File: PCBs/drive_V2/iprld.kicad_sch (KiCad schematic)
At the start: 77 parts, among them IC1 W25Q16JVUXIQ_TR, IC2 ADS1115IDGSR, J1 SM06B-GHS-TB_LF__SN_, J10 XT60PW-F, J12 TYPE-C-31-M-12, J2 SM06B-GHS-TB_LF__SN_, J3 SM06B-GHS-TB_LF__SN_, J4 SM06B-GHS-TB_LF__SN_, J5 SM06B-GHS-TB_LF__SN_, J6 XT60PW-F, J7 SM06B-GHS-TB_LF__SN_, J8 XT60PW-F, J9 XT30PW-F, U1 AMS1117-3.3, U11 4N35, U12 4N35, U13 4N35, U14 4N35, U2 ESP32-S3, U3 4N35, U4 USBLC6-4SC6, U5 TCA9548APWR, U6 4N35, U7 4N35, U8 4N35, U9 AMS1117-5.0, Y1 7M40000010

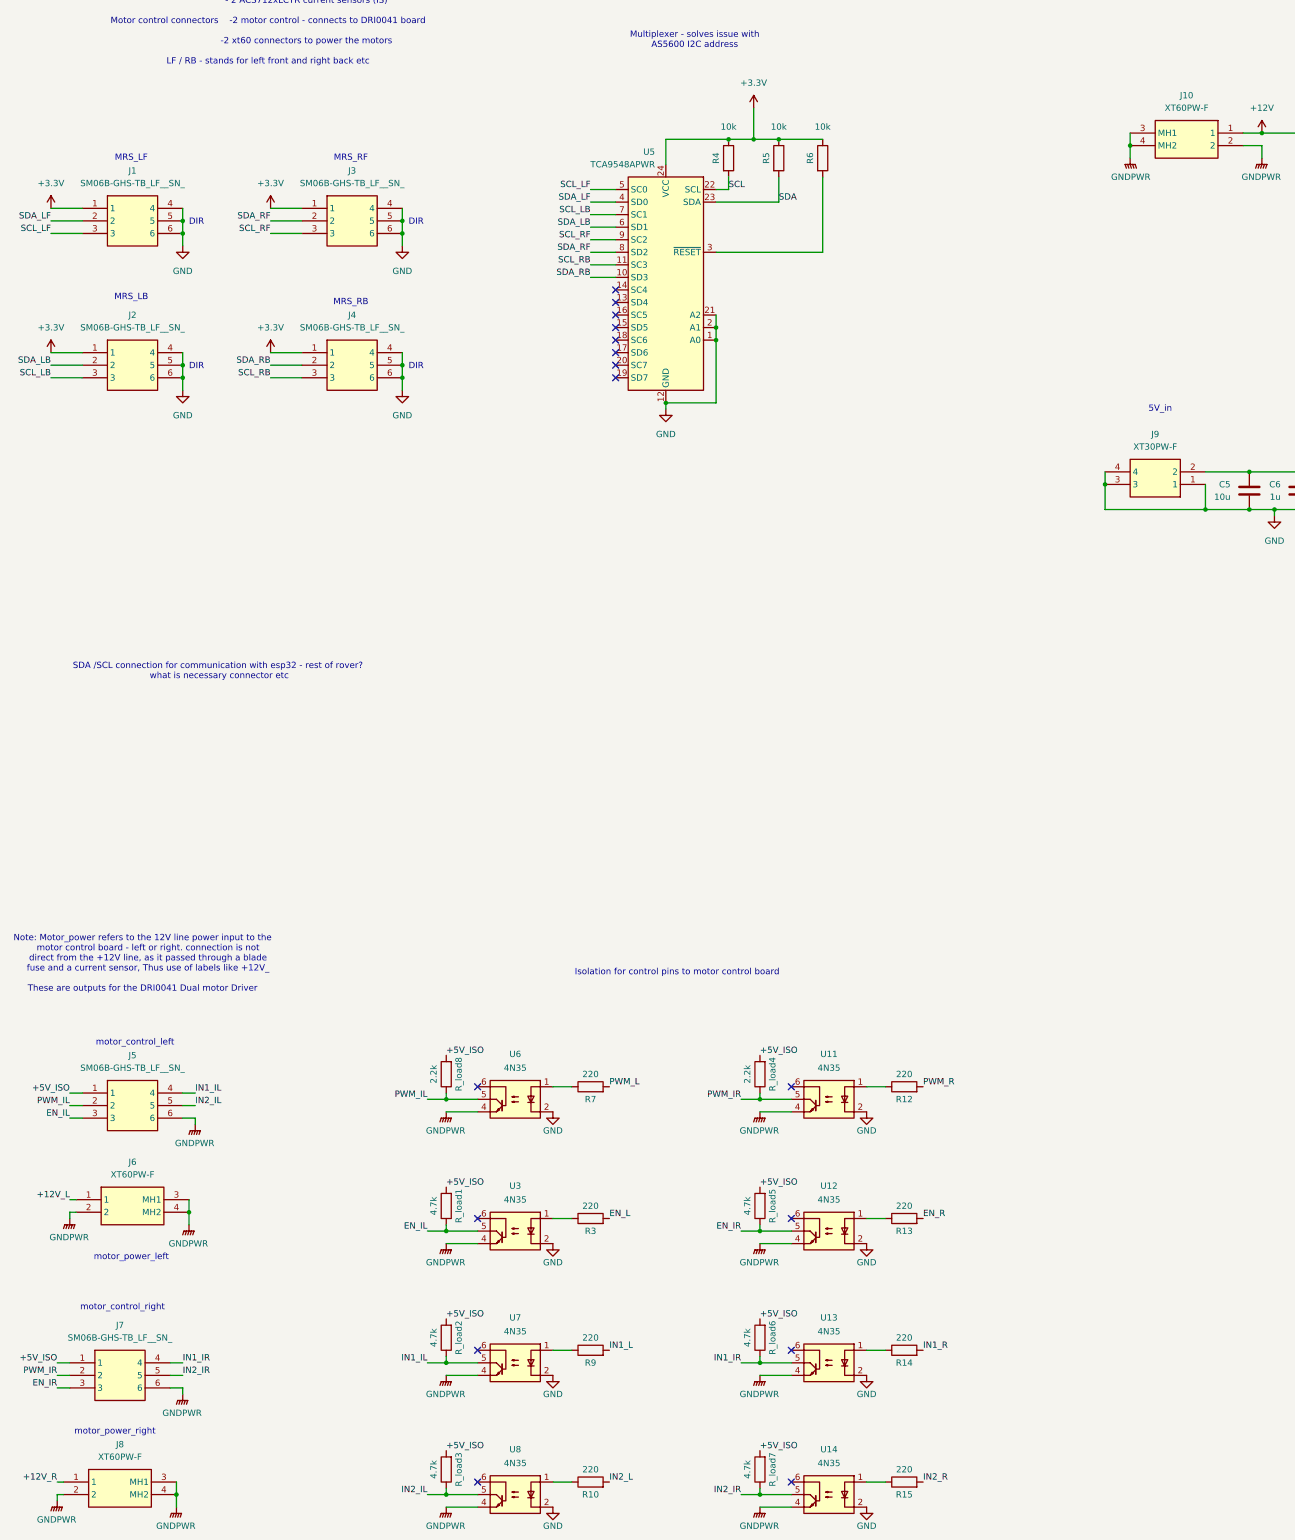
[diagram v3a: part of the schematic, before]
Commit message: added connector names
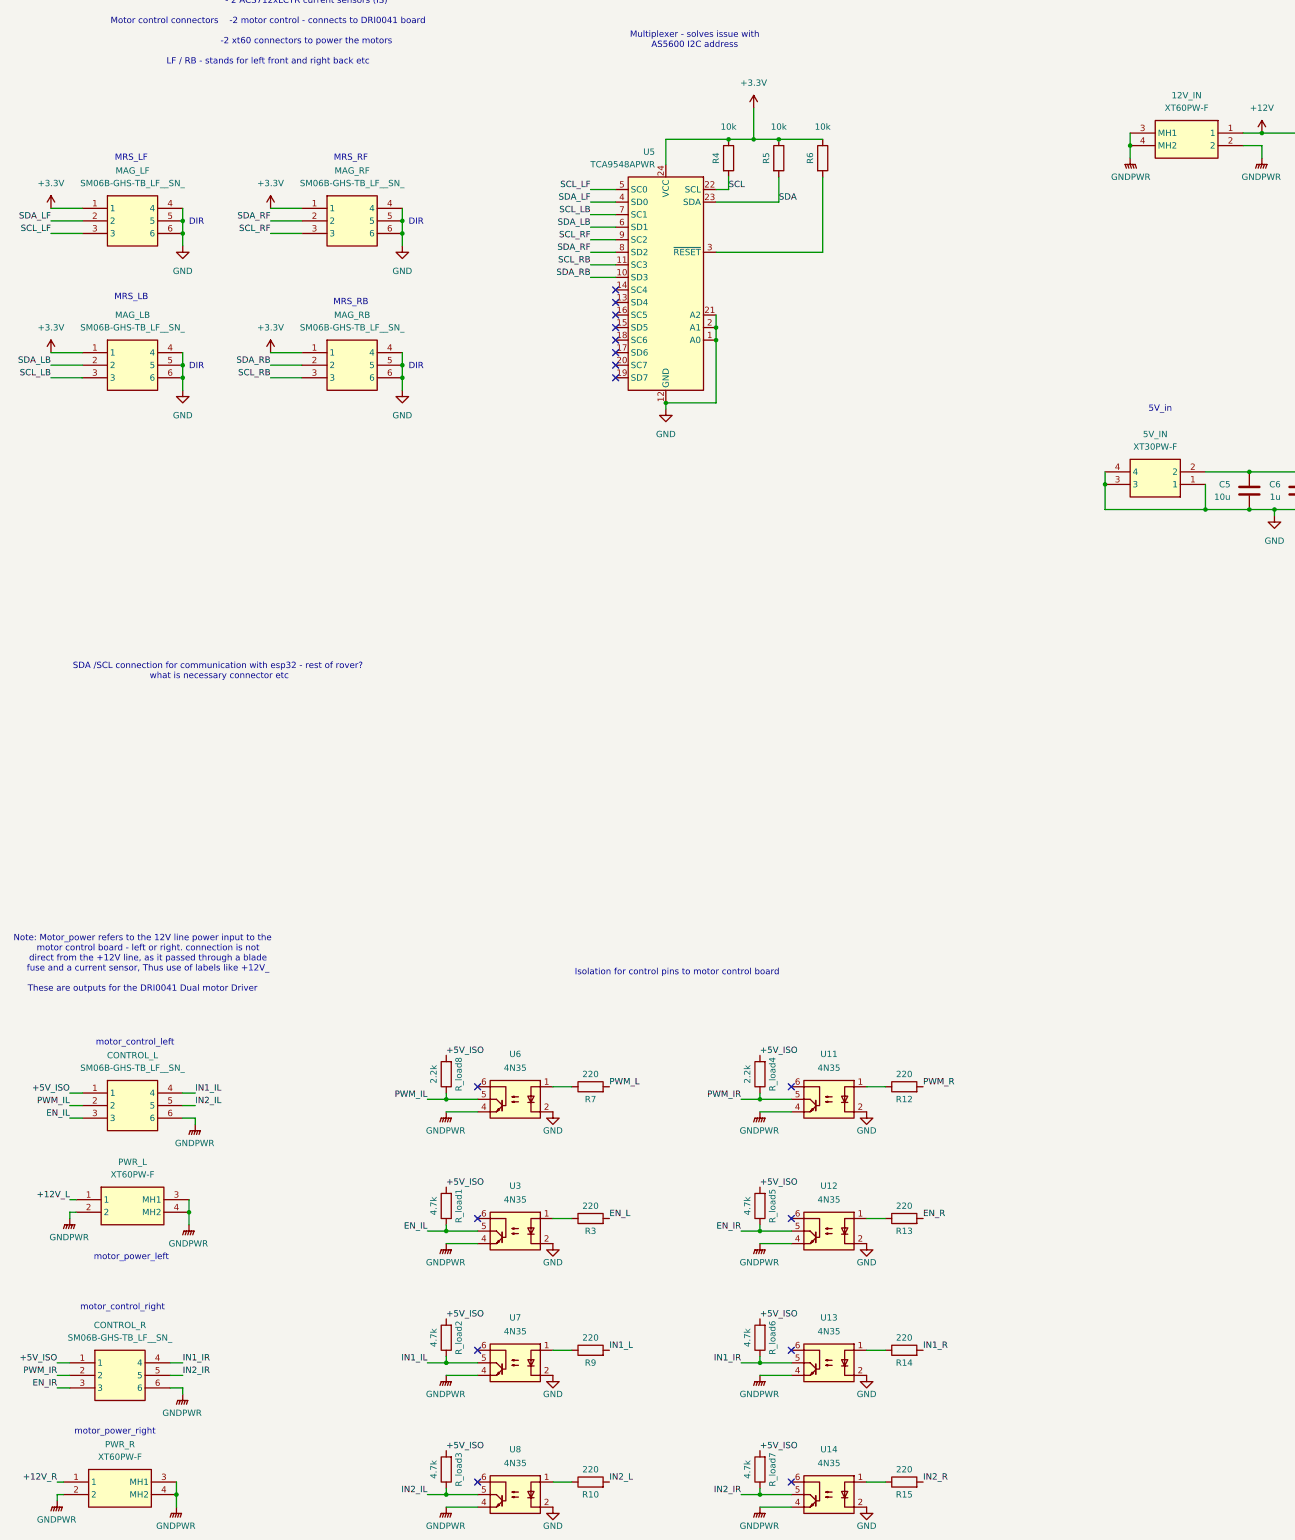
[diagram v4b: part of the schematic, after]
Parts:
- renumbered J10 to 12V_IN, J9 to 5V_IN, J5 to CONTROL_L, J7 to CONTROL_R, J2 to MAG_LB, J1 to MAG_LF, J4 to MAG_RB, J3 to MAG_RF, J6 to PWR_L, J8 to PWR_R
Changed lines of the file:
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@@
 		(on_board yes)
 		(dnp no)
-		(property "Reference" "J8"
+		(property "Reference" "PWR_R"
 			(at 57.15 342.9 0)
 			(effects
@@
 			(project "iprld"
 				(path "/f88582ba-beb9-4fb5-aa18-f7c4bf4c6866"
-					(reference "J8")
+					(reference "PWR_R")
 					(unit 1)
 				)
@@
 		(dnp no)
 		(fields_autoplaced yes)
-		(property "Reference" "J9"
+		(property "Reference" "5V_IN"
 			(at 266.7 138.43 0)
 			(effects
@@
 			(project "iprld"
 				(path "/f88582ba-beb9-4fb5-aa18-f7c4bf4c6866"
-					(reference "J9")
+					(reference "5V_IN")
 					(unit 1)
 				)
@@
 		(dnp no)
 		(fields_autoplaced yes)
-		(property "Reference" "J3"
+		(property "Reference" "MAG_RF"
 			(at 104.14 85.09 0)
 			(effects
@@
 			(project "iprld"
 				(path "/f88582ba-beb9-4fb5-aa18-f7c4bf4c6866"
-					(reference "J3")
+					(reference "MAG_RF")
 					(unit 1)
 				)
@@
 		(dnp no)
 		(fields_autoplaced yes)
-		(property "Reference" "J7"
+		(property "Reference" "CONTROL_R"
 			(at 57.15 318.77 0)
 			(effects
@@
 			(project "iprld"
 				(path "/f88582ba-beb9-4fb5-aa18-f7c4bf4c6866"
-					(reference "J7")
+					(reference "CONTROL_R")
 					(unit 1)
 				)
@@
 		(dnp no)
 		(fields_autoplaced yes)
-		(property "Reference" "J5"
+		(property "Reference" "CONTROL_L"
 			(at 59.69 264.16 0)
 			(effects
@@
 			(project "iprld"
 				(path "/f88582ba-beb9-4fb5-aa18-f7c4bf4c6866"
-					(reference "J5")
+					(reference "CONTROL_L")
 					(unit 1)
 				)
@@
 		(dnp no)
 		(fields_autoplaced yes)
-		(property "Reference" "J2"
+		(property "Reference" "MAG_LB"
 			(at 59.69 114.3 0)
 			(effects
@@
 			(project "iprld"
 				(path "/f88582ba-beb9-4fb5-aa18-f7c4bf4c6866"
-					(reference "J2")
+					(reference "MAG_LB")
 					(unit 1)
 				)
@@
 		(dnp no)
 		(fields_autoplaced yes)
-		(property "Reference" "J4"
+		(property "Reference" "MAG_RB"
 			(at 104.14 114.3 0)
 			(effects
@@
 			(project "iprld"
 				(path "/f88582ba-beb9-4fb5-aa18-f7c4bf4c6866"
-					(reference "J4")
+					(reference "MAG_RB")
 					(unit 1)
 				)
@@
 		(dnp no)
 		(fields_autoplaced yes)
-		(property "Reference" "J1"
+		(property "Reference" "MAG_LF"
 			(at 59.69 85.09 0)
 			(effects
@@
 			(project "iprld"
 				(path "/f88582ba-beb9-4fb5-aa18-f7c4bf4c6866"
-					(reference "J1")
+					(reference "MAG_LF")
 					(unit 1)
 				)
@@
 		(on_board yes)
 		(dnp no)
-		(property "Reference" "J10"
+		(property "Reference" "12V_IN"
 			(at 273.05 69.85 0)
 			(effects
@@
 			(project "iprld"
 				(path "/f88582ba-beb9-4fb5-aa18-f7c4bf4c6866"
-					(reference "J10")
+					(reference "12V_IN")
 					(unit 1)
 				)
@@
 		(on_board yes)
 		(dnp no)
-		(property "Reference" "J6"
+		(property "Reference" "PWR_L"
 			(at 59.69 285.75 0)
 			(effects
@@
 			(project "iprld"
 				(path "/f88582ba-beb9-4fb5-aa18-f7c4bf4c6866"
-					(reference "J6")
+					(reference "PWR_L")
 					(unit 1)
 				)

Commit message: Fixed some DRC errors
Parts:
- removed J12: TYPE-C-31-M-12, main_lib:TYPE-C-31-M-12, symbol TYPE-C-31-M-12:TYPE-C-31-M-12
- added J1: TYPE-C-31-M-12, iprl_footprints:TYPE-C-31-M-12, symbol TYPE-C-31-M-12:TYPE-C-31-M-12
- renumbered 12V_IN to 12V_IN1, 5V_IN to 5V_IN1, CONTROL_L to CONTROL_L1, CONTROL_R to CONTROL_R1, MAG_LB to MAG_LB1, MAG_LF to MAG_LF1, MAG_RB to MAG_RB1, MAG_RF to MAG_RF1, PWR_L to PWR_L1, PWR_R to PWR_R1
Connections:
- net D+: now also J1.A6 (DP1), J1.B6 (DP2)
- net D-: now also J1.A7 (DN1), J1.B7 (DN2)
- net GND: now also J1.A1_B12 (GND), J1.B1_A12 (GND), J1.S1 (SHIELD), J1.S2 (SHIELD), J1.S3 (SHIELD), J1.S4 (SHIELD)
- net VBUS: now also J1.A4_B9 (VBUS), J1.B4_A9 (VBUS)
- net at R20.2: now also J1.A5 (CC1)
- net at R21.2: now also J1.B5 (CC2)

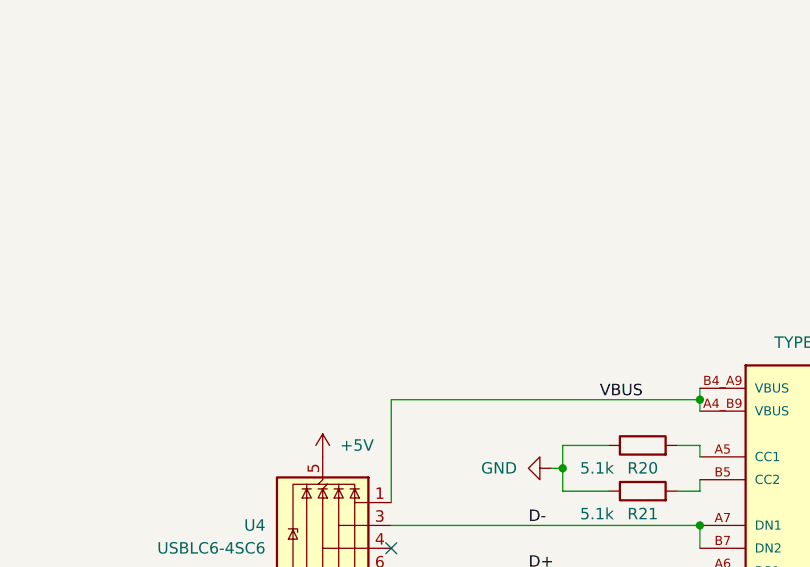
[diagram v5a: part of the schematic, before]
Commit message: Found some issues in the drive schematic and PCB
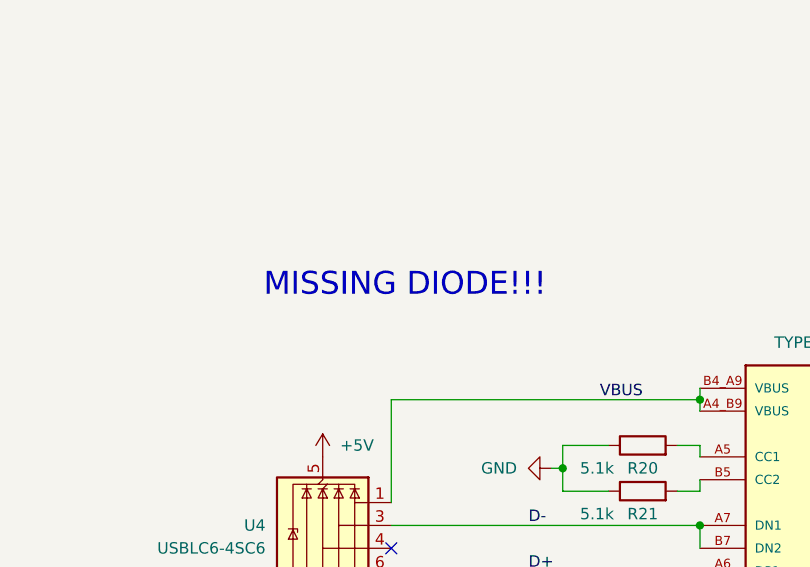
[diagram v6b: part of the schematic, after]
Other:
- note added: "MISSING DIODE!!!"
